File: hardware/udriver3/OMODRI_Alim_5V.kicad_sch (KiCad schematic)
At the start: 8 parts, among them U11 TPSM5601R5

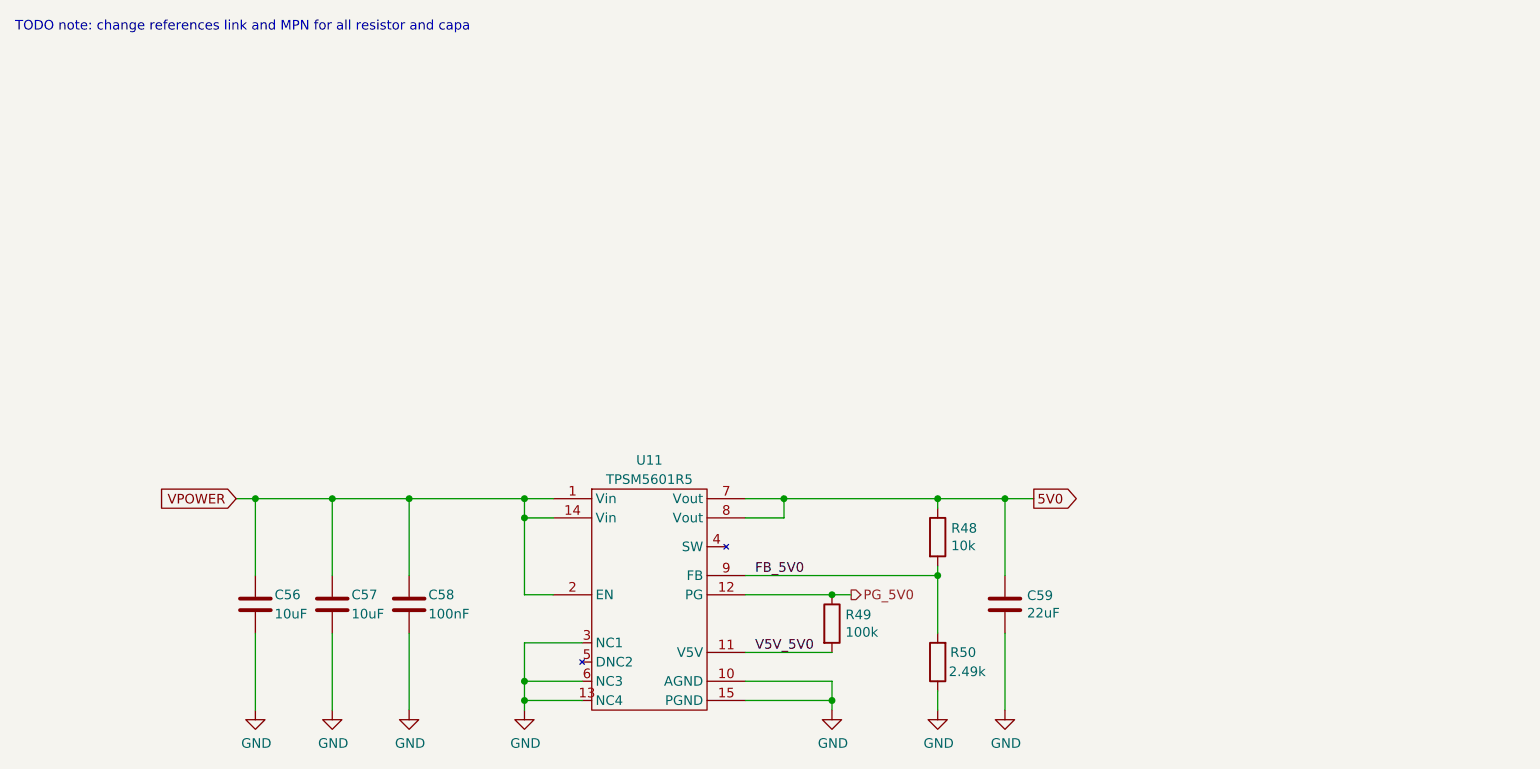
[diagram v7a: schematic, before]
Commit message: Schematics updates (DC/DC description).
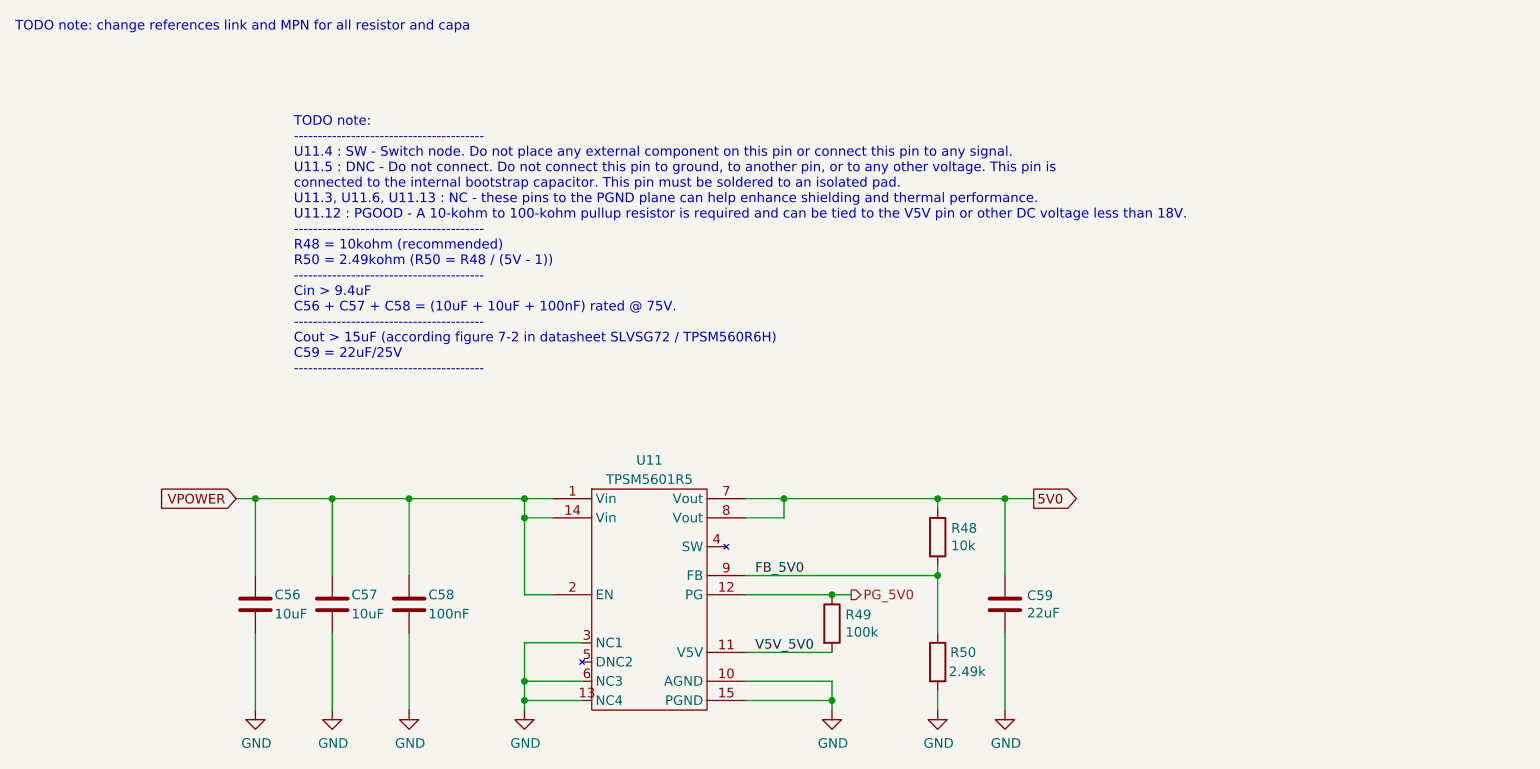
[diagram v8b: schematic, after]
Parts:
- R50: DigiKey P122907TR-ND -> P122865TR-ND; Farnell 3335262 -> 3335222; Mouser 667-ERJ-1GNF2941C -> 667-ERJ-1GNF2491C; Part No ERJ-1GNF2941C -> ERJ-1GNF2491C
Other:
- note added: "TODO note: ---------------------------------------- U11.4 : SW - Switch node. Do not place any external component on this pin or connect this pin to any signal. U11.5 : DNC - Do not connect. Do not connect this pin to ground, to another pin, or to any other voltage. This pin is connected to the internal bootstrap capacitor. This pin must be soldered to an isolated pad. U11.3, U11.6, U11.13 : NC -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"
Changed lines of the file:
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@@
+    (effects (font (size 1.27 1.27)) (justify left bottom))
+  )
+  (text "TODO note:\n----------------------------------------\nU11.4 : SW - Switch node. Do not place any external component on this pin or connect this pin to any signal.\nU11.5 : DNC - Do not connect. Do not connect this pin to ground, to another pin, or to any other voltage. This pin is\nconnected to the internal bootstrap capacitor. This pin must be soldered to an isolated pad.\nU11.3, U11.6, U11.13 : NC - these pins to the PGND plane can help enhance shielding and thermal performance.\nU11.12 : PGOOD - A 10-kohm to 100-kohm pullup resistor is required and can be tied to the V5V pin or other DC voltage less than 18V.\n----------------------------------------\nR48 = 10kohm (recommended)\nR50 = 2.49kohm (R50 = R48 / (5V - 1))\n----------------------------------------\nCin > 9.4uF\nC56 + C57 + C58 = (10uF + 10uF + 100nF) rated @ 75V.\n----------------------------------------\nCout > 15uF (according figure 7-2 in datasheet SLVSG72 / TPSM560R6H)\nC59 = 22uF/25V\n----------------------------------------\n\n\n\n"
+    (at 93.98 72.39 0)
     (effects (font (size 1.27 1.27)) (justify left bottom))
   )
@@
       (effects (font (size 1.27 1.27)) hide)
     )
-    (property "DigiKey" "P122907TR-ND" (id 4) (at 179.07 104.14 0)
-      (effects (font (size 1.27 1.27)) hide)
-    )
-    (property "Farnell" "3335262" (id 5) (at 179.07 104.14 0)
-      (effects (font (size 1.27 1.27)) hide)
-    )
-    (property "Mouser" "667-ERJ-1GNF2941C" (id 6) (at 179.07 104.14 0)
-      (effects (font (size 1.27 1.27)) hide)
-    )
-    (property "Part No" "ERJ-1GNF2941C" (id 7) (at 179.07 104.14 0)
-      (effects (font (size 1.27 1.27)) hide)
-    )
+    (property "DigiKey" "P122865TR-ND" (id 4) (at 179.07 104.14 0)
+      (effects (font (size 1.27 1.27)) hide)
+    )
+    (property "Farnell" "3335222" (id 5) (at 179.07 104.14 0)
+      (effects (font (size 1.27 1.27)) hide)
+    )
+    (property "Mouser" "667-ERJ-1GNF2491C" (id 6) (at 179.07 104.14 0)
+      (effects (font (size 1.27 1.27)) hide)
+    )
+    (property "Part No" "ERJ-1GNF2491C" (id 7) (at 179.07 104.14 0)
+      (effects (font (size 1.27 1.27)) hide)
+    )
